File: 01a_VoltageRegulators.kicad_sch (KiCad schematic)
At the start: 40 parts, among them U5 TPS54331, U6 TPS51396Ax, U7 TLV75733PDBV, U8 TLV75733PDBV

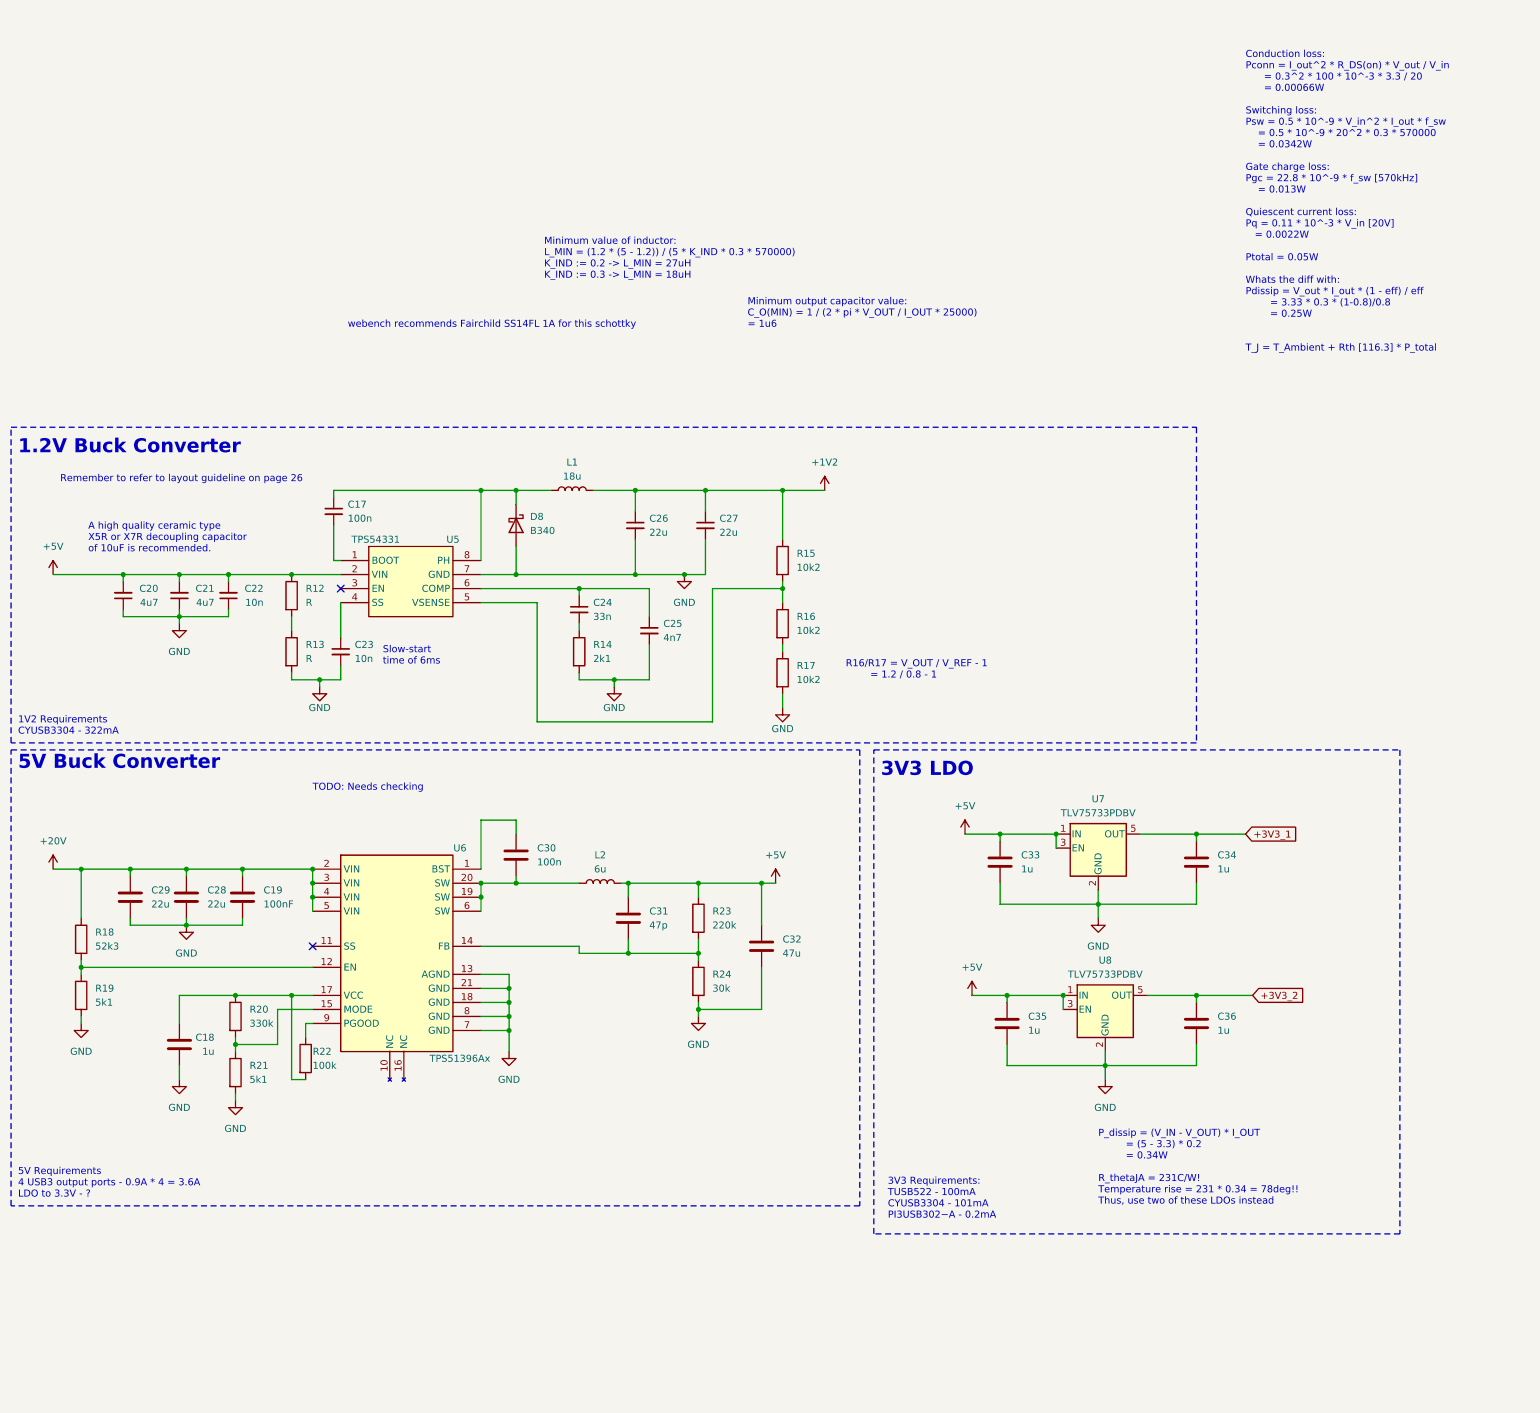
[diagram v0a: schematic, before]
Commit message: add usb hub controller schematic, fix up redriver
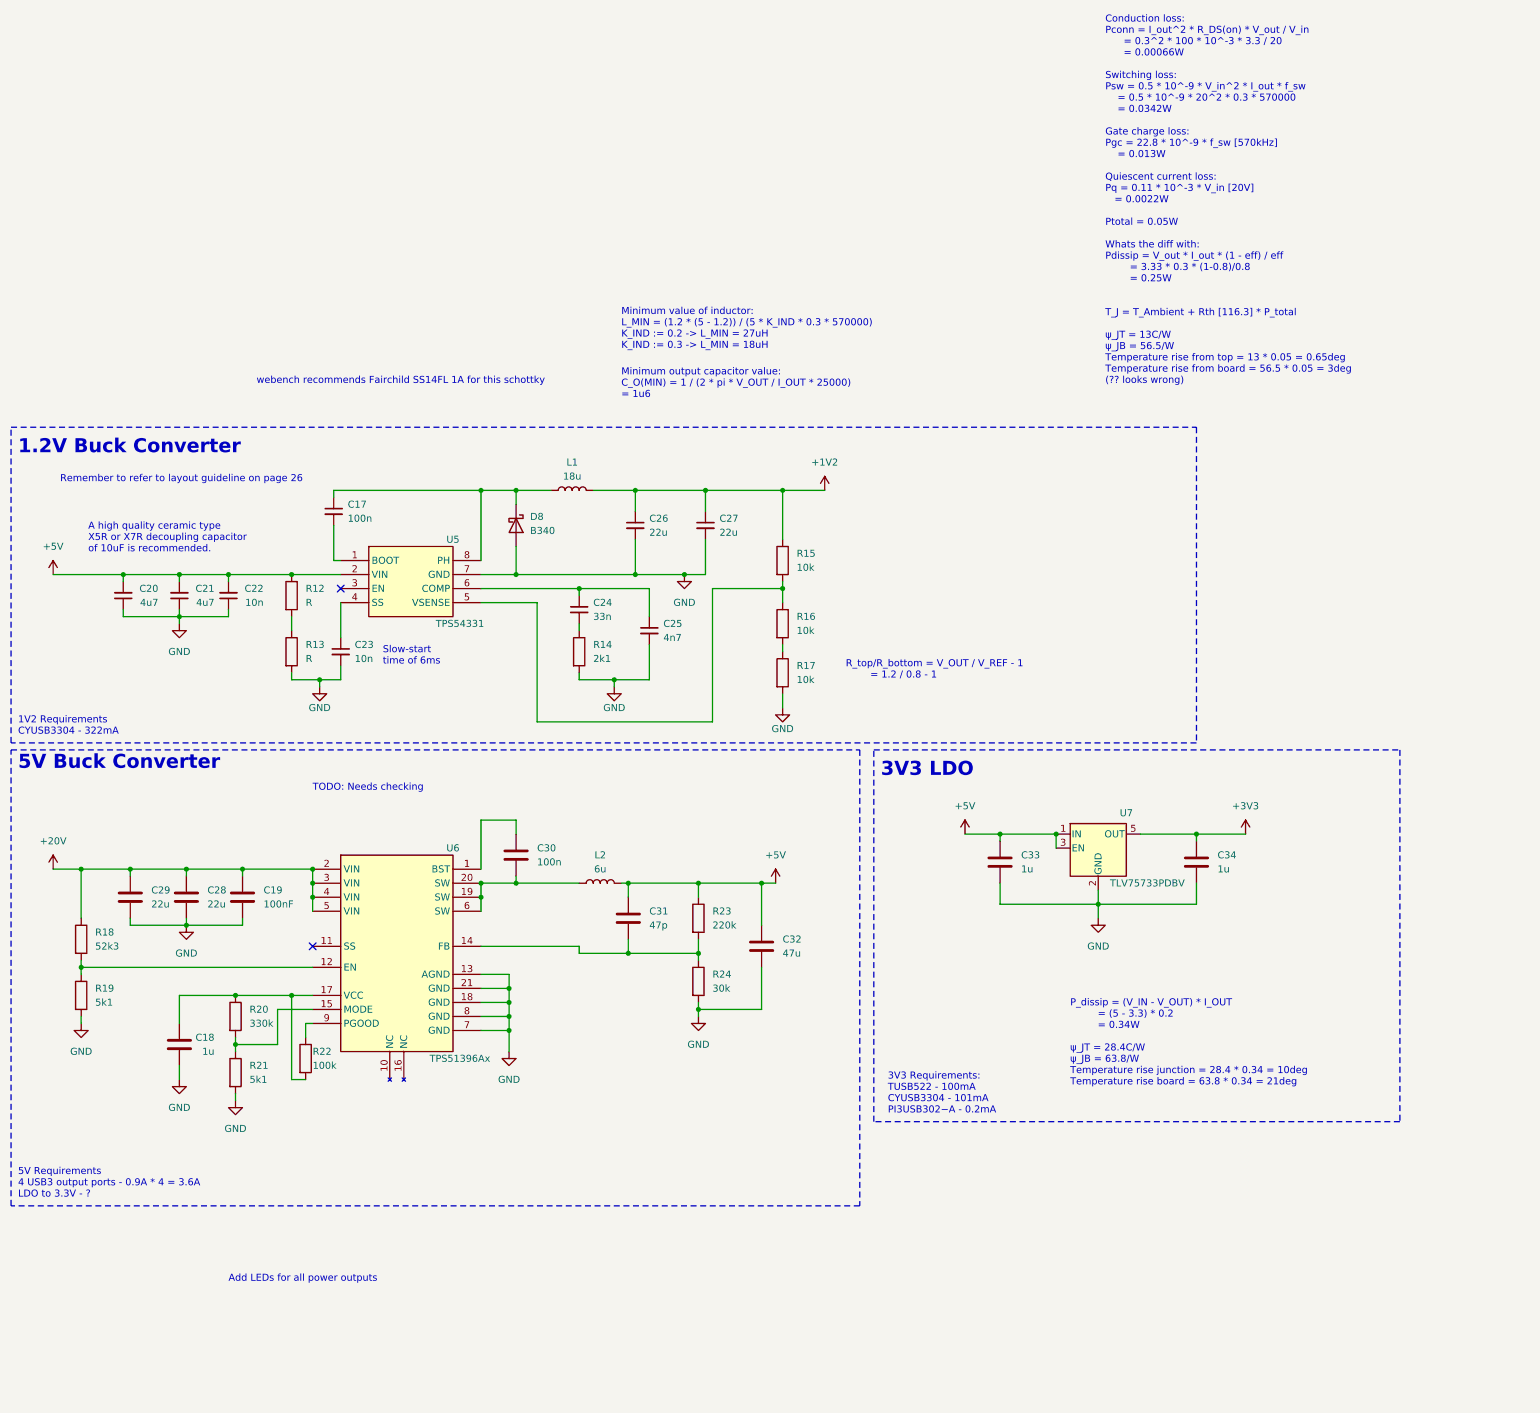
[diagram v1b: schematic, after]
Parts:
- removed C35, C36: 1u, symbol Device:C
- removed U8: TLV75733PDBV, Package_TO_SOT_SMD:SOT-23-5, symbol Regulator_Linear:TLV75733PDBV
- R15, R16, R17: value 10k2 -> 10k
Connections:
- net +3V3_1 renamed +3V3
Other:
- note added: "Add LEDs for all power outputs"
- note added: "P_dissip = (V_IN - V_OUT) * I_OUT = (5 - 3.3) * 0.2 = 0.34W ψ_JT = 28.4C/W ψ_JB = 63.8/W Temperature rise junction = 28.4 * 0.34 = 10deg Temperature rise board = 63.8 * 0.34 = 21deg"
- note added: "R_top/R_bottom = V_OUT / V_REF - 1 = 1.2 / 0.8 - 1"
- note removed: "P_dissip = (V_IN - V_OUT) * I_OUT = (5 - 3.3) * 0.2 = 0.34W R_thetaJA = 231C/W! Temperature rise = 231 * 0.34 = 78deg!! Thus, use two of these LDOs instead"
- note removed: "R16/R17 = V_OUT / V_REF - 1 = 1.2 / 0.8 - 1"

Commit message: WIP hub and DFP
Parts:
- removed R12, R13: R, symbol Device:R
- added D10: GREEN, LED_SMD:LED_0603_1608Metric, symbol Device:LED
- added R30: 5k1, Resistor_SMD:R_0603_1608Metric, symbol Device:R
- C24: value 33n -> 6n8
- C25: value 4n7 -> 6p8
- R14: value 2k1 -> 6k65
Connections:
- net +5V: now also D10.2 (A)
- net GND: now also C24.2, R30.2; no longer R14.2
- net at C25.1, U5.6 (COMP): now also R14.1; no longer C24.1
- new net: D10.1 (K), R30.1
- new net: C24.1, R14.2
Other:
- note added: "5V LED"
- note added: "Slow-start time of 4ms"
- note removed: "Add LEDs for all power outputs"
- note removed: "Slow-start time of 6ms"
- moved on the sheet: C23, C24, R14

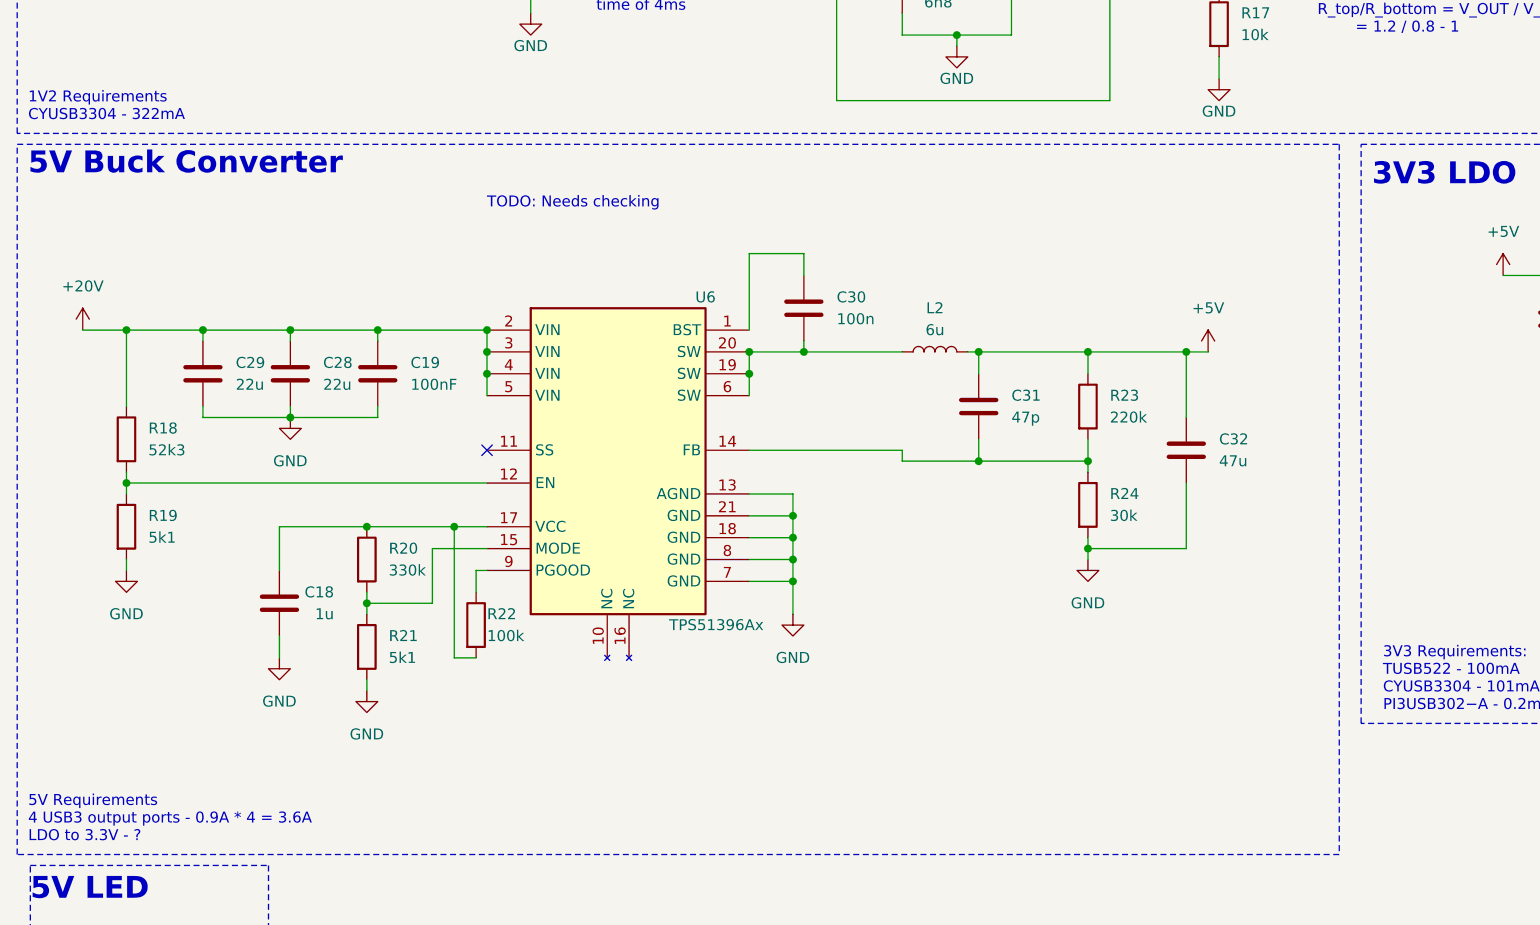
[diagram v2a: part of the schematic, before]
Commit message: use simpler buck for 5V
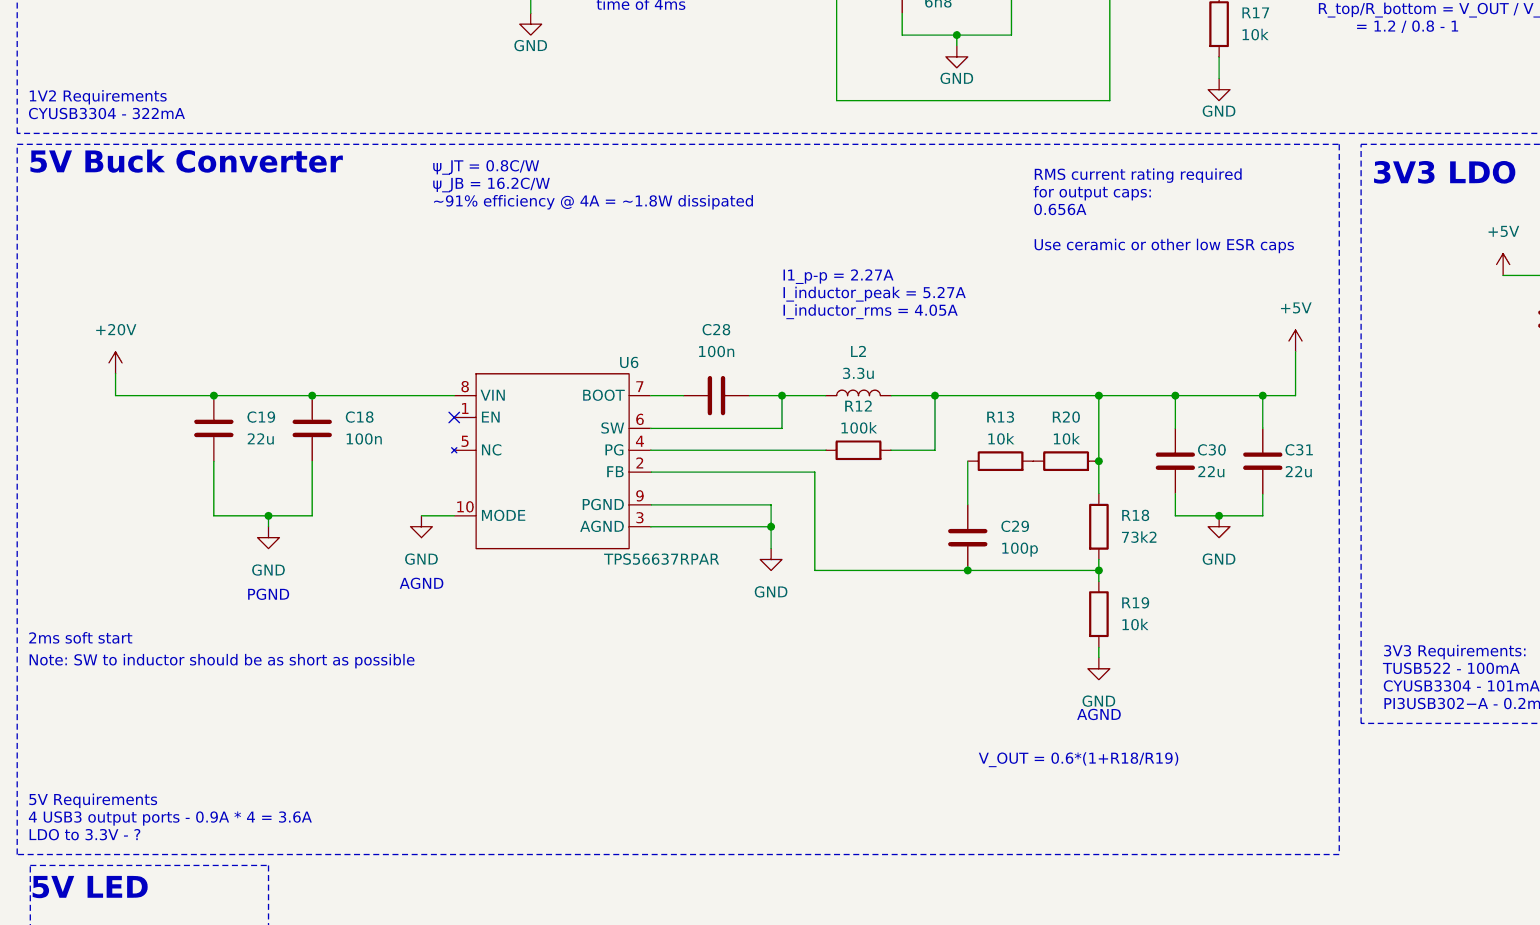
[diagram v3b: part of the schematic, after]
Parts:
- removed C32: 47u, symbol Device:C
- removed R21: 5k1, symbol Device:R
- removed R22: 100k, symbol Device:R
- removed R23: 220k, symbol Device:R
- removed R24: 30k, symbol Device:R
- removed U6: TPS51396Ax, Cake_USB:TPS51396Ax, symbol CakeUSB:TPS51396Ax
- added R12: 100k, symbol Device:R
- added R13: 10k, symbol Device:R
- added U6: TPS56637RPAR, symbol CakeUSB:TPS56637RPAR
- C18: value 1u -> 100n
- C19: value 100nF -> 22u
- C28: value 22u -> 100n
- C29: value 22u -> 100p
- C30: value 100n -> 22u
- C31: value 47p -> 22u
- L2: value 6u -> 3.3u
- R18: value 52k3 -> 73k2
- R19: value 5k1 -> 10k
- R20: value 330k -> 10k
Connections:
- net +20V: now also C18.1, U6.8 (VIN); no longer C28.1, C29.1, R18.1
- net +5V: now also C30.1, R18.1, R20.2, R12.2
- net GND: now also C18.2, C30.2, C31.2, U6.10 (MODE), U6.3 (AGND), U6.9 (PGND); no longer C18.1, C28.2, C29.2
- net at R20.1: now also R13.2; no longer C18.2
- net at L2.1: now also C28.2, U6.6 (SW); no longer C30.2
- net at R18.2, R19.1: now also C29.2, U6.2 (FB)
- new net: R12.1, U6.4 (PG)
- new net: C28.1, U6.7 (BOOT)
- new net: C29.1, R13.1
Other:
- note added: "2ms soft start"
- note added: "AGND"
- note added: "I1_p-p = 2.27A I_inductor_peak = 5.27A I_inductor_rms = 4.05A"
- note added: "Note: SW to inductor should be as short as possible"
- note added: "PGND"
- note added: "RMS current rating required for output caps: 0.656A Use ceramic or other low ESR caps"
- note added: "V_OUT = 0.6*(1+R18/R19)"
- note added: "ψ_JT = 0.8C/W ψ_JB = 16.2C/W ~91% efficiency @ 4A = ~1.8W dissipated"
- note removed: "TODO: Needs checking"
